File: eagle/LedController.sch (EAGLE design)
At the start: 20 parts, among them IC2 MEGA8-P, IC3 7805, Q1 16MHz, Q2 FDS8884, Q3 FDS8884, Q4 FDS8884, X1 2510-, X2 MKDSN1,5/4-5,08

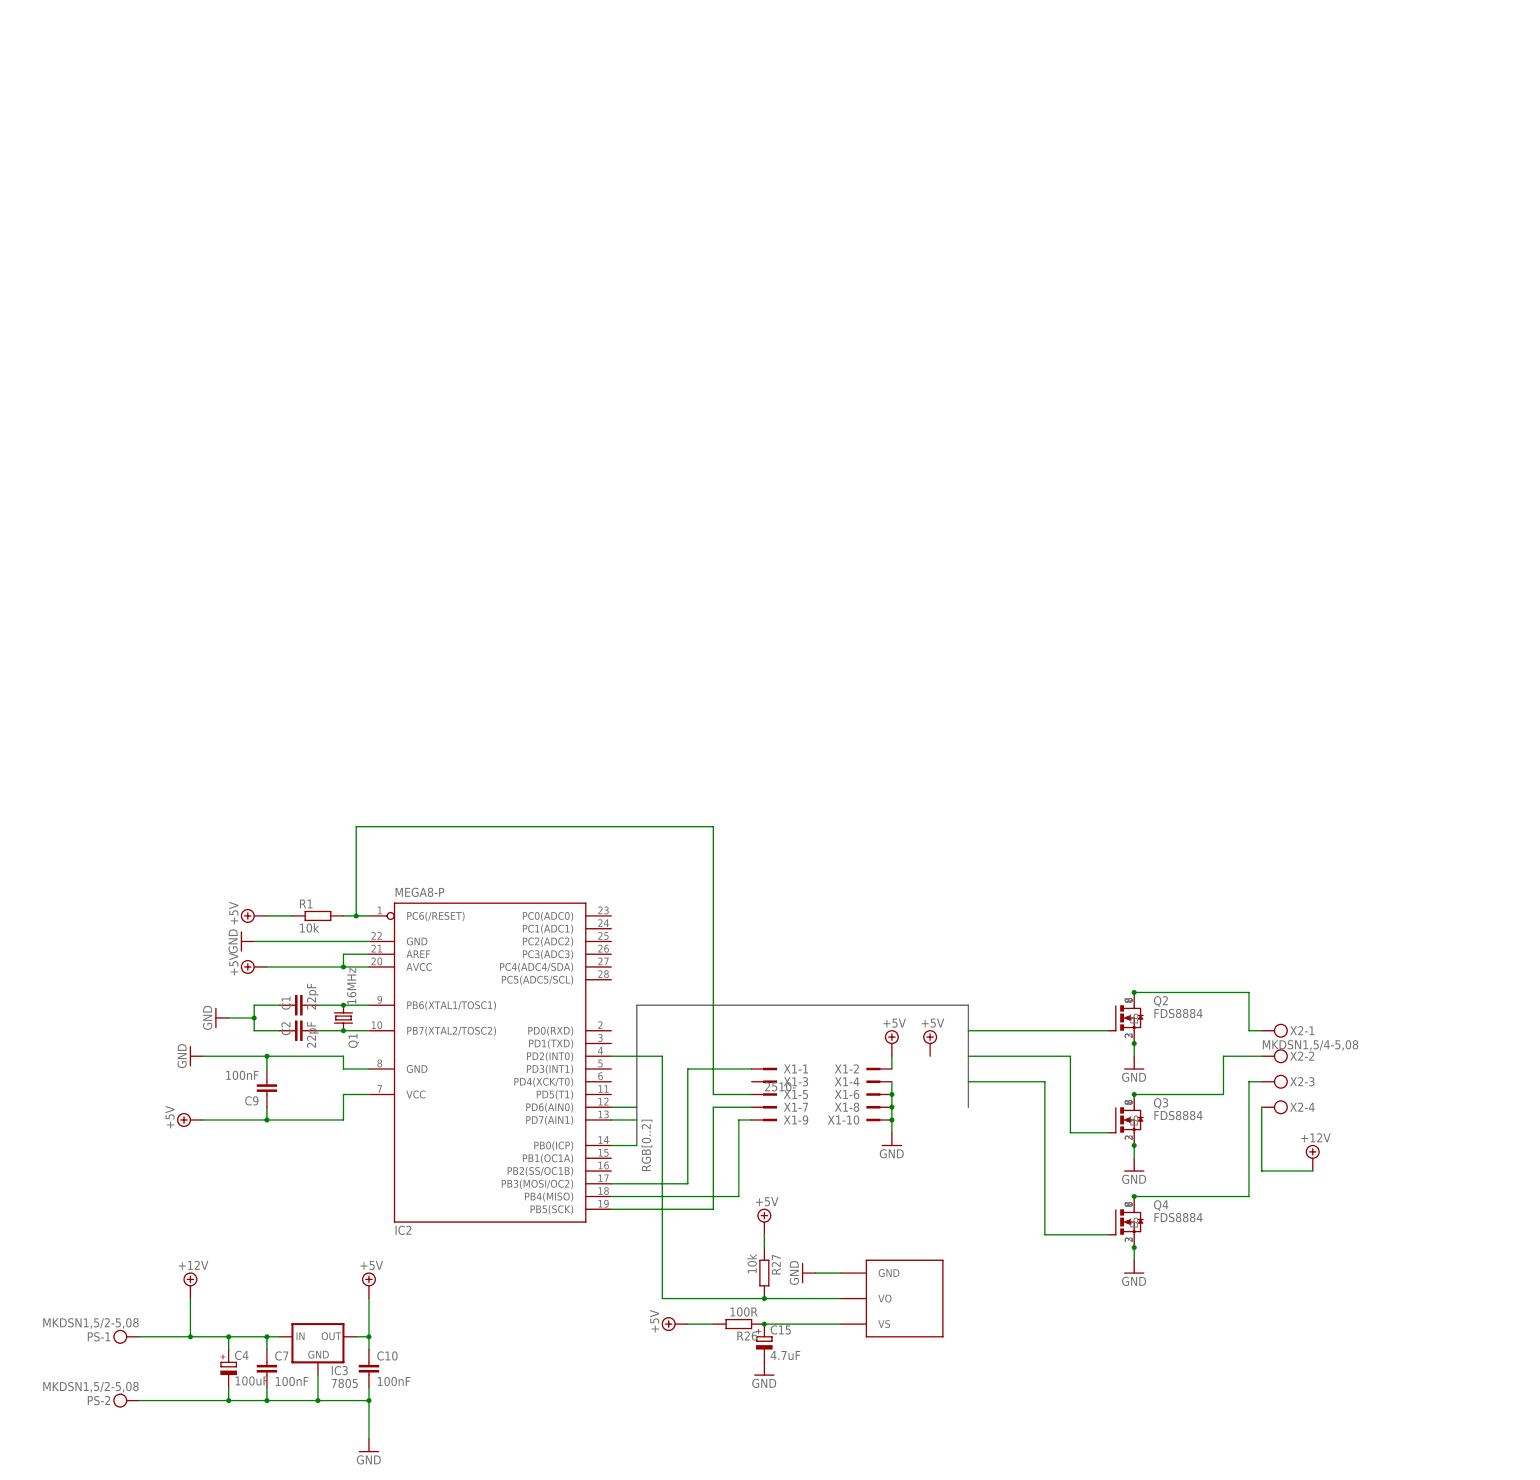
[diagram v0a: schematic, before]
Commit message: Add reverse polarity protection
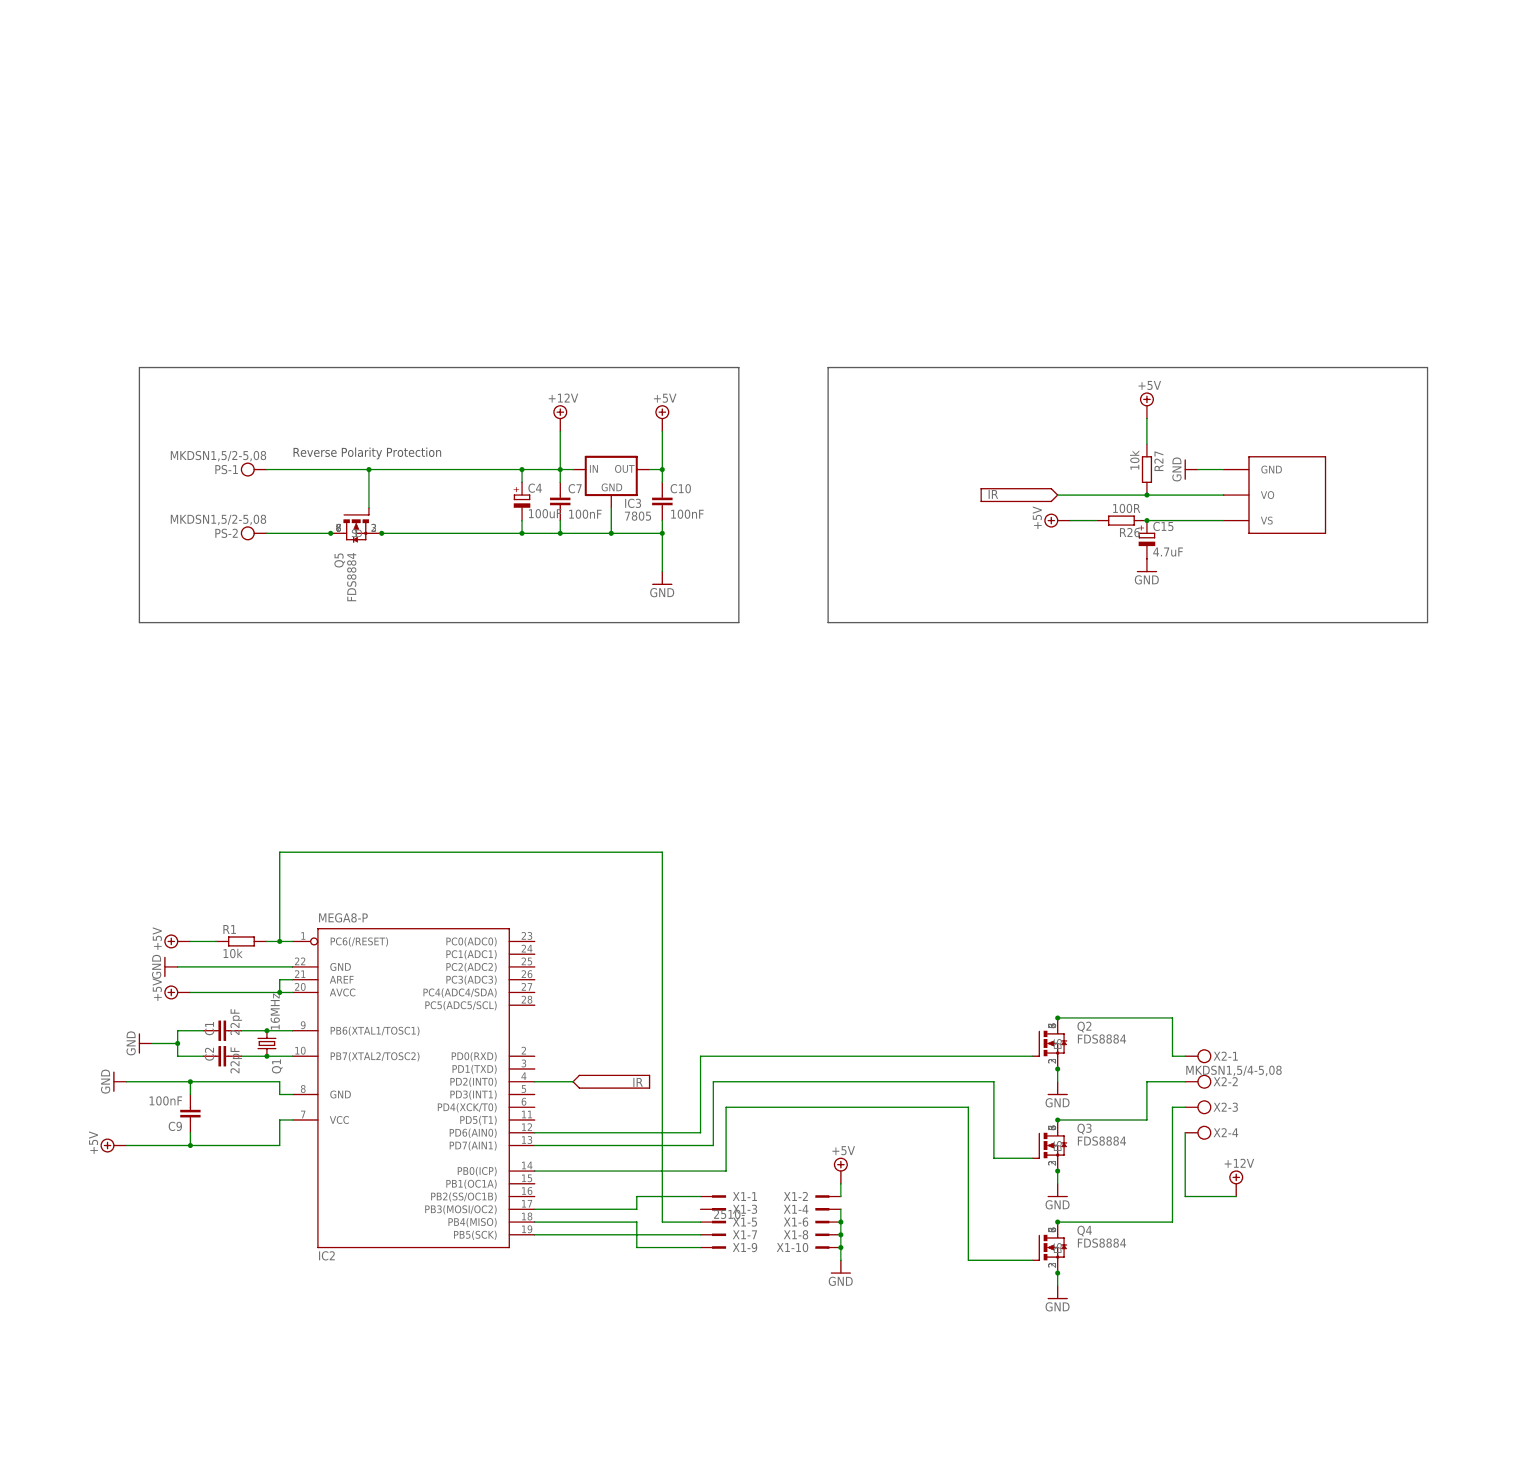
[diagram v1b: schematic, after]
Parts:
- removed U$1: TSOP, TSOP1736:TSOP
- added Q5: FDS8884, FDS8884:FDS8884
- added TSOP: TSOP, TSOP1736:TSOP
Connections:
- removed net N$62: IC2.PD2(INT0), R27.2, U$1.VO
- new net IR: IC2.PD2(INT0), R27.2, TSOP.VO
- new net N$8: PS-2.KL, Q5.D, Q5.D@1, Q5.D@2, Q5.D@3
- net +12V: now also Q5.G
- net GND: now also Q5.S, Q5.S@1, Q5.S@2, TSOP.GND; no longer PS-2.KL, U$1.GND
- net N$63: now also TSOP.VS; no longer U$1.VS
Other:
- note added: "Reverse Polarity Protection"
- moved on the sheet: C1, C10, C15, C2, C4, C7, C9, IC2, IC3, PS-1, PS-2, Q1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

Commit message: Changing Signal Names, split up into individual parts in schematic
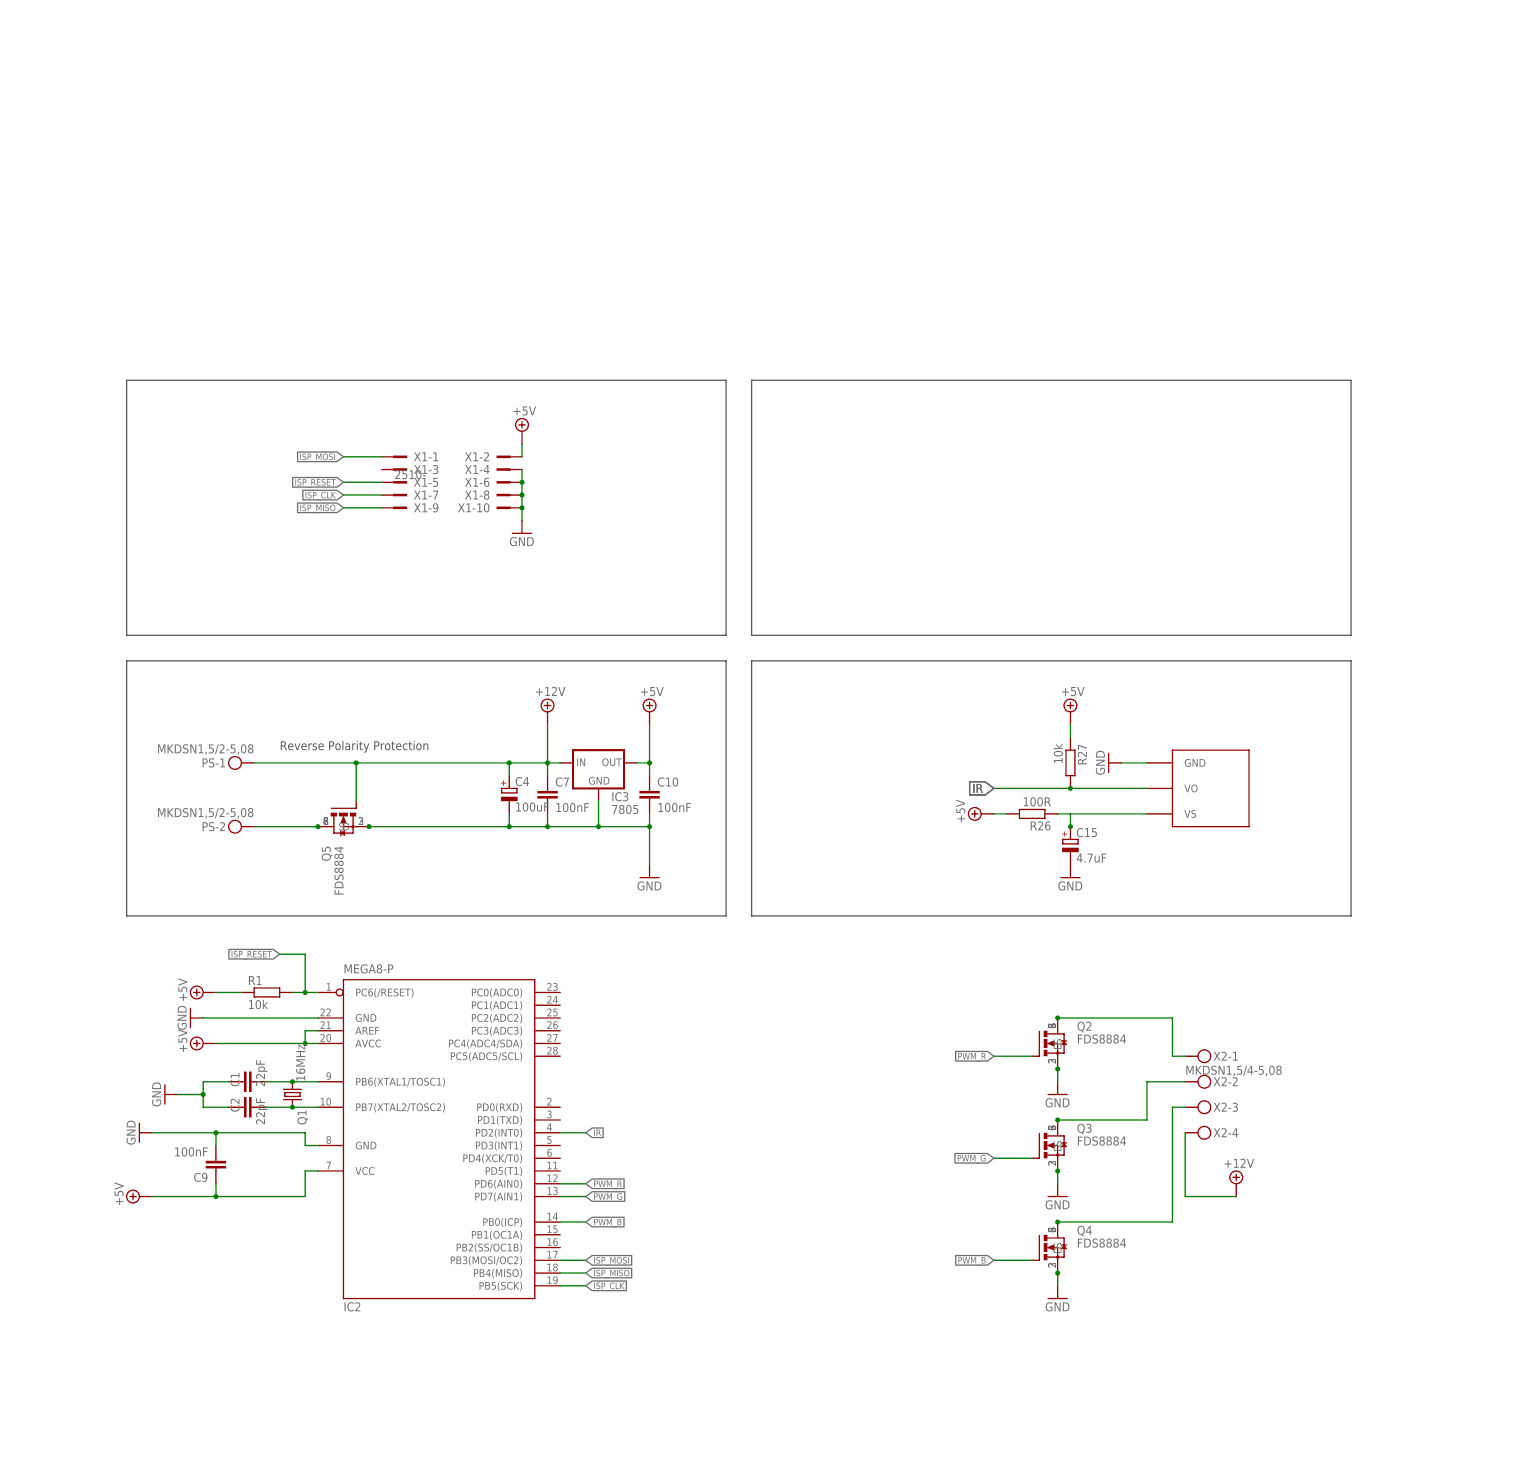
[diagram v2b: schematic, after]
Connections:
- net N$1 renamed ISP_MOSI
- net N$54 renamed ISP_CLK
- net N$7 renamed ISP_RESET
- net N$71 renamed ISP_MISO
- net RGB0 renamed PWM_R
- net RGB1 renamed PWM_G
- net RGB2 renamed PWM_B
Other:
- moved on the sheet: C1, C10, C15, C2, C4, C7, C9, IC2, IC3, PS-1, PS-2, Q1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

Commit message: add preamp stage for microphone
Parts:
- added C3: 100nF, rcl:C-EU025-025X050
- added C5: 1uF, rcl:C-EU025-024X044
- added C6: 4n7, rcl:C-EU025-024X044
- added IC1: MCP601R, linear:MCP601R
- added R2: 100, rcl:R-EU_0207/2V
- added R3, R4: 1k, rcl:R-EU_0207/2V
- added R5, R6, R7: 10k, rcl:R-EU_0207/2V
- added R8: 12k, rcl:R-EU_0207/2V
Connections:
- new net ADC: C6.2, IC2.PC0(ADC0), R8.2
- new net N$1: C5.1, R3.1
- new net N$10: IC1.-IN, R4.1
- new net N$11: IC1.+IN, R5.2, R6.1
- new net N$12: IC1.OUT, R7.2, R8.1
- new net N$7: C3.1, IC2.AREF, IC2.AVCC, R2.1
- new net N$9: C5.2, R4.2, R7.1
- net +5V: now also IC1.V+, R2.2, R3.2, R5.1; no longer IC2.AREF, IC2.AVCC
- net GND: now also C3.2, C6.1, IC1.V-, R6.2
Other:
- moved on the sheet: C10, C15, C4, C7, IC3, PS-1, PS-2, Q5, R26, R27, X1-1, X1-10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
